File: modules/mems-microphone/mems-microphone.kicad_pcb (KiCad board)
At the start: 2 copper layers, 10.1 x 12.7 mm, 2 parts

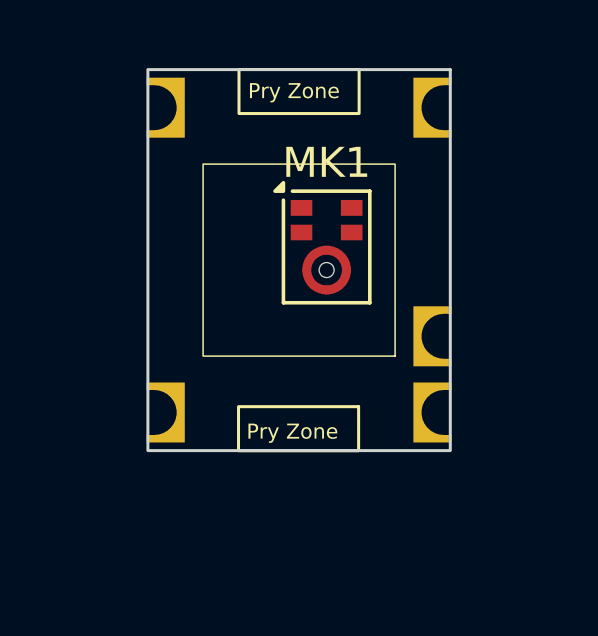
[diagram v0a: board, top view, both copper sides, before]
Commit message: add footprints for passives for MEMS mic module
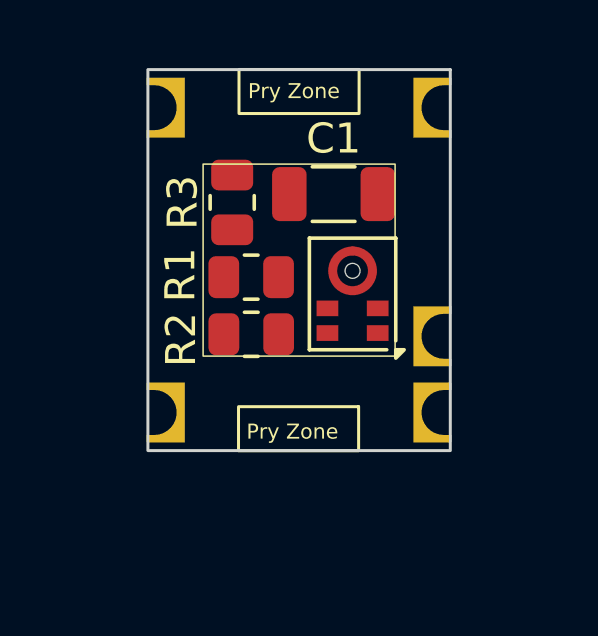
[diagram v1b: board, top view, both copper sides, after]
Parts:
- added C1: 100nF, Capacitor_SMD:C_1206_3216Metric, F.Cu at (63.1, 45.7)
- added R1: 100, Resistor_SMD:R_0805_2012Metric, F.Cu at (60.3, 50.4)
- added R2: 100, Resistor_SMD:R_0805_2012Metric, F.Cu at (60.3, 48.5)
- added R3: 100K, Resistor_SMD:R_0805_2012Metric, F.Cu at (59.7, 46.0)
- moved MK1 1.79 mm to (63.7, 49.0), turned to 180 degrees

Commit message: use 0603 resistors to make it all fit
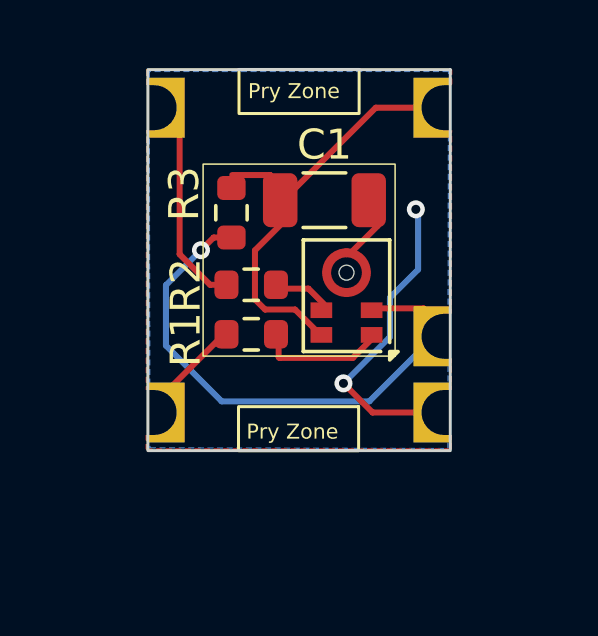
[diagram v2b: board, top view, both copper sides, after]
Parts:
- R1, R2, R3: footprint Resistor_SMD:R_0805_2012Metric -> Resistor_SMD:R_0603_1608Metric
- moved C1 0.37 mm to (62.8, 45.9)
- moved R3 0.35 mm to (59.7, 46.3)
- moved R2 0.25 mm to (60.3, 48.7)
- moved MK1 0.21 mm to (63.5, 49.1)
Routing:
- net LR_SELECT: track 0.00 -> 19.3 mm, vias 0 -> 1
- net VCC: track 0.00 -> 15.6 mm
- net GND: track 0.00 -> 13.1 mm, vias 0 -> 2
- net CLOCK: track 0.00 -> 7.68 mm
- net Net-(MK1-DATA): track 0.00 -> 4.42 mm
- net DATA: track 0.00 -> 3.67 mm
- net Net-(MK1-CLOCK): track 0.00 -> 2.01 mm
- added copper zone on B.Cu, net GND
- added copper zone on F.Cu, net GND

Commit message: save changes to mems microphone module
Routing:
- net GND: track 13.1 -> 14.8 mm
- removed copper zone on F.Cu, net GND
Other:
- board text added: "20250211"
- board text added: "MEMS Mic"
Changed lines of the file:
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@@
 		(tags "MEMS Microphone LGA")
 		(property "Reference" "MK1"
-			(at 0 -2.8 360)
+			(at 0 -2.8 0)
 			(layer "F.SilkS")
 			(hide yes)
@@
 		(tags "capacitor")
 		(property "Reference" "C1"
-			(at 0 -1.85 360)
+			(at 0 -1.85 0)
 			(layer "F.SilkS")
 			(effects
@@
 		)
 		(property "Footprint" "Capacitor_SMD:C_1206_3216Metric"
-			(at 0 0 360)
+			(at 0 0 0)
 			(layer "F.Fab")
 			(hide yes)
@@
 		)
 		(property "Datasheet" ""
-			(at 0 0 360)
+			(at 0 0 0)
 			(layer "F.Fab")
 			(hide yes)
@@
 		)
 		(property "Description" "Unpolarized capacitor"
-			(at 0 0 360)
+			(at 0 0 0)
 			(layer "F.Fab")
 			(hide yes)
@@
 		)
 		(fp_text user "${REFERENCE}"
-			(at 0 0 360)
+			(at 0 0 0)
 			(layer "F.Fab")
 			(effects
@@
 		(attr smd)
 		(fp_rect
-			(start -1.984241 -4.885886)
-			(end 2.019516 -6.354478)
+			(start -1.984241 -4.8)
+			(end 2.019516 -6.268592)
 			(stroke
 				(width 0.1)
@@
 		)
 		(fp_rect
-			(start -2.000193 6.354102)
-			(end 2.003564 4.88551)
+			(start -2.001878 6.243592)
+			(end 2.001879 4.775)
 			(stroke
 				(width 0.1)
@@
 			(layer "Edge.Cuts")
 		)
-		(fp_text user "Pry Zone"
-			(at 1.755819 -6.011473 0)
+		(fp_text user "PRY"
+			(at 1.1 -6.15 0)
 			(unlocked yes)
 			(layer "F.SilkS")
 			(effects
 				(font
-					(size 0.5 0.5)
+					(size 0.8 0.8)
 					(thickness 0.1)
 				)
@@
 			)
 		)
-		(fp_text user "Pry Zone"
-			(at 1.705127 5.338692 0)
+		(fp_text user "PRY"
+			(at 1.27 5.08 0)
 			(unlocked yes)
 			(layer "F.SilkS")
 			(effects
 				(font
-					(size 0.5 0.5)
+					(size 0.8 0.8)
 					(thickness 0.1)
 				)
@@
 		(pad "1" thru_hole rect
 			(at -5.08 5.08 180)
-			(size 1.27 2)
-			(drill oval 2 1.5
-				(offset 0.635 0)
-			)
+			(size 2.54 2)
+			(drill oval 2 1.5)
 			(property pad_prop_castellated)
 			(layers "*.Cu" "*.Mask")
@@
 		(pad "4" thru_hole rect
 			(at -5.08 -2.54 180)
-			(size 1.27 2)
-			(drill oval 2 1.5
-				(offset 0.635 0)
-			)
+			(size 2.54 2)
+			(drill oval 2 1.5)
 			(property pad_prop_castellated)
 			(layers "*.Cu" "*.Mask")
@@
 		(pad "5" thru_hole rect
 			(at -5.08 -5.08 180)
-			(size 1.27 2)
-			(drill oval 2 1.5
-				(offset 0.635 0)
-			)
+			(size 2.54 2)
+			(drill oval 2 1.5)
 			(property pad_prop_castellated)
 			(layers "*.Cu" "*.Mask")
@@
 		(pad "6" thru_hole rect
 			(at 5.08 5.08 180)
-			(size 1.27 2)
-			(drill oval 2 1.5
-				(offset -0.635 0)
-			)
+			(size 2.54 2)
+			(drill oval 2 1.5)
 			(property pad_prop_castellated)
 			(layers "*.Cu" "*.Mask")
@@
 		(pad "10" thru_hole rect
 			(at 5.08 -5.08 180)
-			(size 1.27 2)
-			(drill oval 2 1.5
-				(offset -0.635 0)
-			)
+			(size 2.54 2)
+			(drill oval 2 1.5)
 			(property pad_prop_castellated)
 			(layers "*.Cu" "*.Mask")
@@
 		)
 	)
+	(gr_text "20250211"
+		(at 58.42 44.45 90)
+		(layer "B.SilkS")
+		(effects
+			(font
+				(size 1 1)
+				(thickness 0.1)
+			)
+			(justify left bottom mirror)
+		)
+	)
+	(gr_text "MEMS Mic"
+		(at 65.675 43.5 0)
+		(layer "B.SilkS")
+		(effects
+			(font
+				(size 1 1)
+				(thickness 0.1)
+			)
+			(justify left bottom mirror)
+		)
+	)
 	(segment
 		(start 56.84 52.9661)
@@
 	)
 	(segment
+		(start 65.8114 46.228)
+		(end 64.545 46.228)
+		(width 0.2)
+		(layer "F.Cu")
+		(net 3)
+	)
+	(segment
 		(start 64.545 46.773)
 		(end 64.545 45.72)
+		(width 0.2)
+		(layer "F.Cu")
+		(net 3)
+	)
+	(segment
+		(start 64.545 46.228)
+		(end 64.2402 45.9232)
 		(width 0.2)
 		(layer "F.Cu")
@@
 	)
 	(zone
-		(net 3)
-		(net_name "GND")
-		(layer "F.Cu")
-		(hatch edge 0.5)
-		(connect_pads
-			(clearance 0.5)
-		)
-		(min_thickness 0.25)
-		(filled_areas_thickness no)
-		(fill yes
-			(thermal_gap 0.5)
-			(thermal_bridge_width 0.5)
-		)
-		(polygon
-			(pts
-				(xy 56.84 41.57) (xy 56.831179 54.226415) (xy 66.991179 54.226415) (xy 67 41.57)
-			)
-		)
-	)
-	(zone
-		(net 3)
-		(net_name "GND")
-		(layer "F.Cu")
-		(hatch edge 0.5)
-		(priority 1)
-		(connect_pads
-			(clearance 0.5)
-		)
-		(min_thickness 0.25)
-		(filled_areas_thickness no)
-		(fill yes
-			(thermal_gap 0.5)
-			(thermal_bridge_width 0.5)
-		)
-		(polygon
-			(pts
-				(xy 56.84 41.57) (xy 56.831179 54.226415) (xy 66.991179 54.226415) (xy 67 41.57)
-			)
-		)
-	)
-	(zone

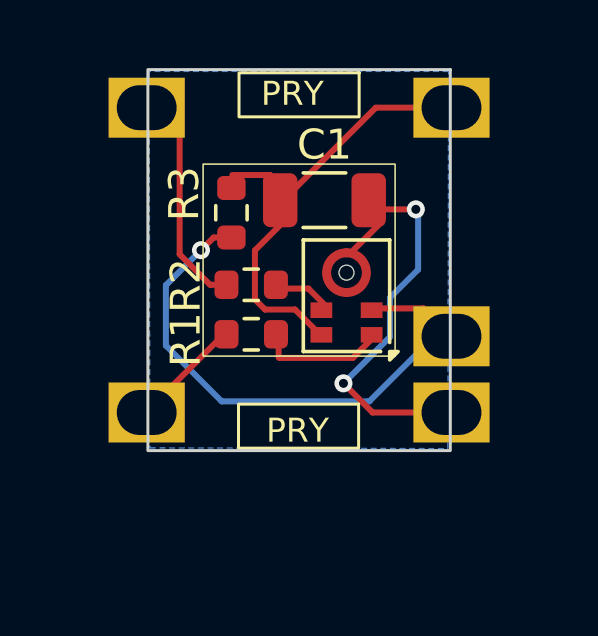
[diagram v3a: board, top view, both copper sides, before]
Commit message: update footprint for mems microphone
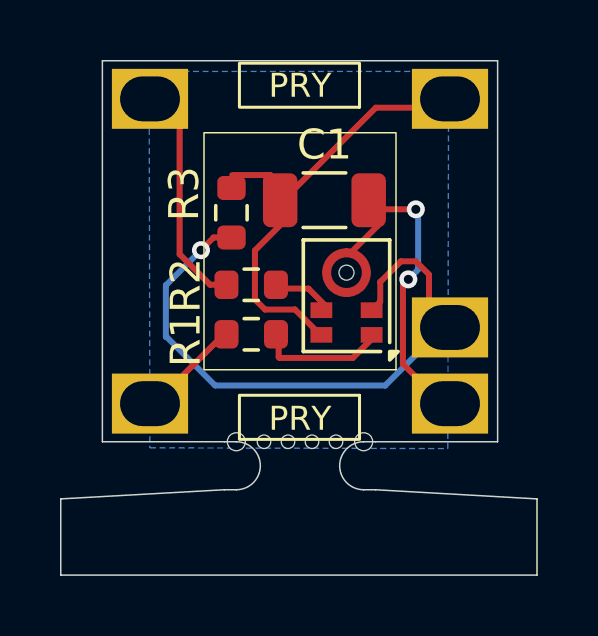
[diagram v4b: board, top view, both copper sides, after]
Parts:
- M1: footprint MegaCastle:MegaCastle2x5-Module-M9C4 -> MegaCastle:MegaCastle2x5-Module-I6.4x7.9-M9C4-PANEL-NIBBLE
- moved M1 0.30 mm to (62.0, 47.6)
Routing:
- net GND: track 14.8 -> 11.6 mm
- net LR_SELECT: track 19.3 -> 22.4 mm
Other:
- board size 10.1 x 12.7 mm -> 13.2 x 14.3 mm
